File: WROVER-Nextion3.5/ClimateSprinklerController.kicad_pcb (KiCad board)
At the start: 2 copper layers, 136.5 x 54.9 mm, 120 parts, among them J1 USB_B_Micro, J2 7.5 TO 40 V, J3 NEXTION, J4 SERIAL, J5 SPI, J6 PIR, J7 I2C, Q1 MMSS8050, Q2 MMSS8050, Q3 TEPT5700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

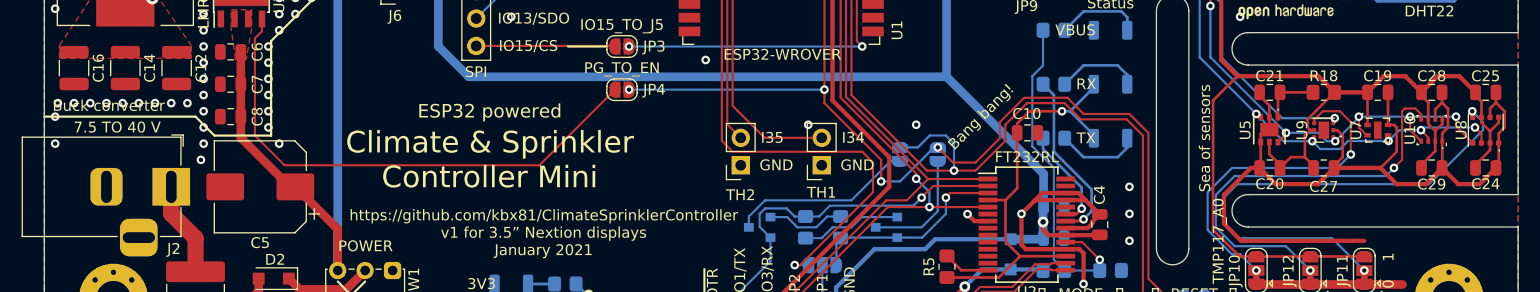
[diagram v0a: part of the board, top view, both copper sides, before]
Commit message: Nextion PCBs tweak
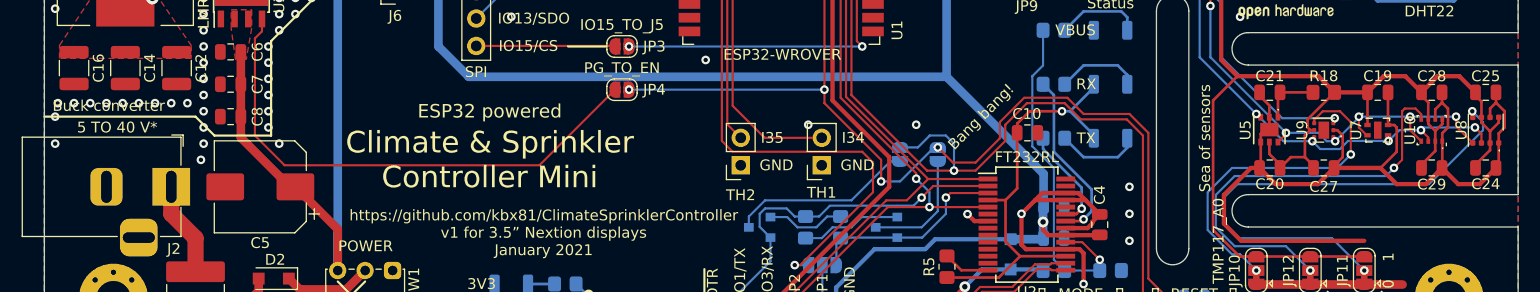
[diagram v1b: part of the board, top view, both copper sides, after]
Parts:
- J2: value 7.5 TO 40 V -> 5 TO 40 V*

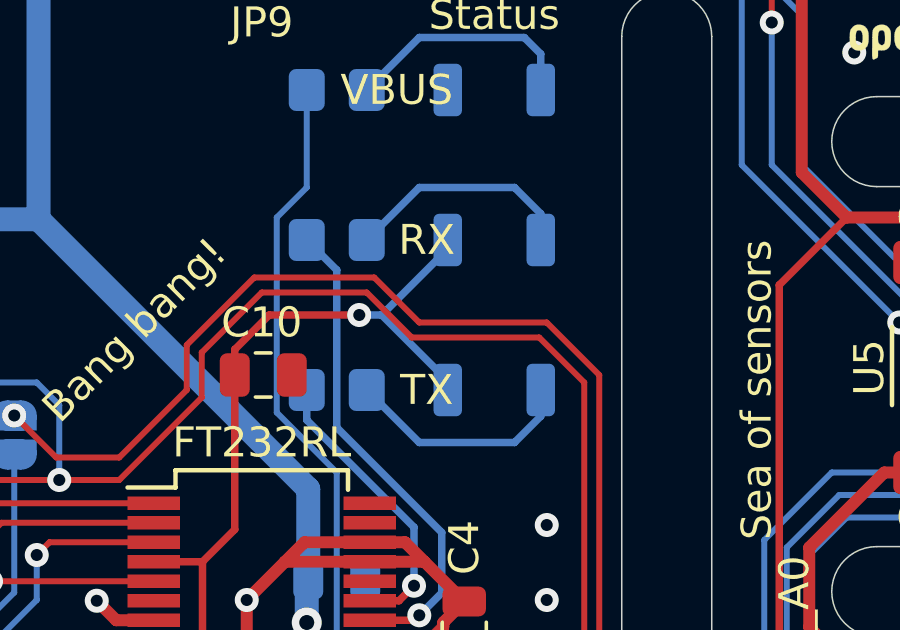
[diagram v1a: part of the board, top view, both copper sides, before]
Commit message: TX+RX LEDs were backwards...oops
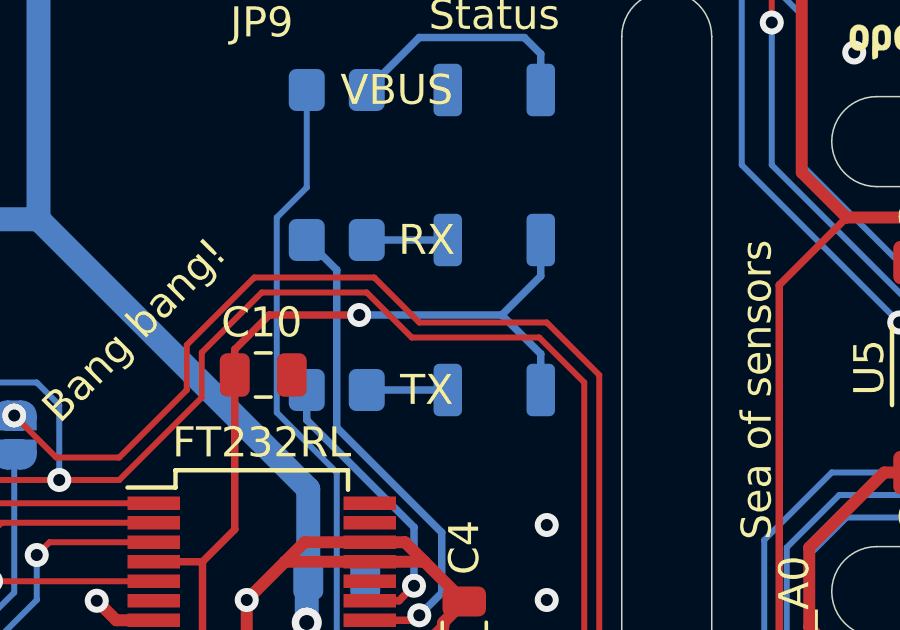
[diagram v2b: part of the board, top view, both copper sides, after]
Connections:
- D3 pad 1: Net-(C10-Pad1) -> Net-(D3-Pad1)
- D3 pad 2: Net-(D3-Pad2) -> Net-(C10-Pad1)
- D4 pad 1: Net-(C10-Pad1) -> Net-(D4-Pad1)
- D4 pad 2: Net-(D4-Pad2) -> Net-(C10-Pad1)
- R3 pad 1: Net-(D3-Pad2) -> Net-(D3-Pad1)
- R4 pad 1: Net-(D4-Pad2) -> Net-(D4-Pad1)
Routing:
- net Net-(D4-Pad2): track 7.76 -> 0.00 mm
- net Net-(D3-Pad2): track 7.76 -> 0.00 mm
- net Net-(C10-Pad1): track 38.9 -> 42.2 mm
- net Net-(D4-Pad1): track 0.00 -> 2.70 mm
- net Net-(D3-Pad1): track 0.00 -> 2.70 mm

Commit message: Doc updates, new images, new enclosures, regenerate gerbers
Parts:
- D1, D2: value MBR230S1F-7 -> N/A
- J1: value USB_B_Micro -> N/A
- TH1, TH2: value NXFT15XH103FA2B100 -> 10K
- U5: value SGP40-Sensor_Air_Quality -> SGP40
- moved REF** 15.9 mm to (212.6, 81.5)
- moved U11 7.66 mm to (206.1, 82.0)
- moved C22 7.32 mm to (129.0, 67.1)
- moved C31 7.01 mm to (195.7, 79.5), turned to 270 degrees
- moved C5 1.19 mm to (101.7, 101.9)
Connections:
- C31 pad 1: +5V -> +3V3
- U11 pad 1: +5V -> +3V3
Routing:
- net +5V: track 233.4 -> 187.1 mm
- net +3V3: track 317.5 -> 349.8 mm, vias 2 -> 1
- net /DHT_DATA: track 64.2 -> 59.5 mm
- net Net-(JP4-Pad2): track 48.5 -> 49.6 mm
- net GND: vias 70 -> 71
